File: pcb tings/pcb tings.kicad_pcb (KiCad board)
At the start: 2 copper layers, 24 parts, among them SW1 SW_Push, U1 ATmega32U4-A, Y1 16MHz

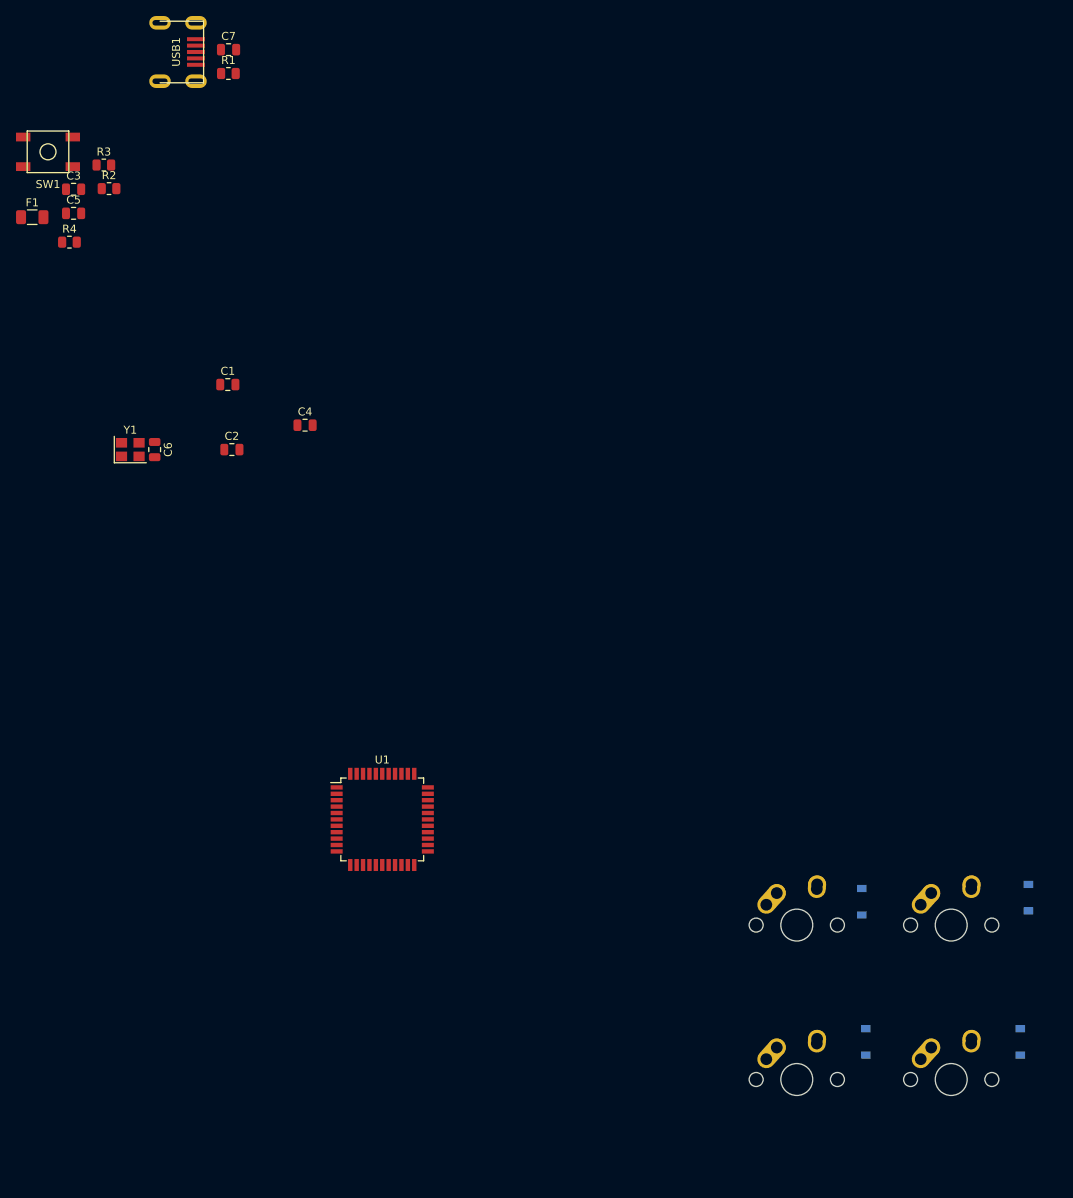
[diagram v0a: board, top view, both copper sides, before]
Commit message: completing the component placements.
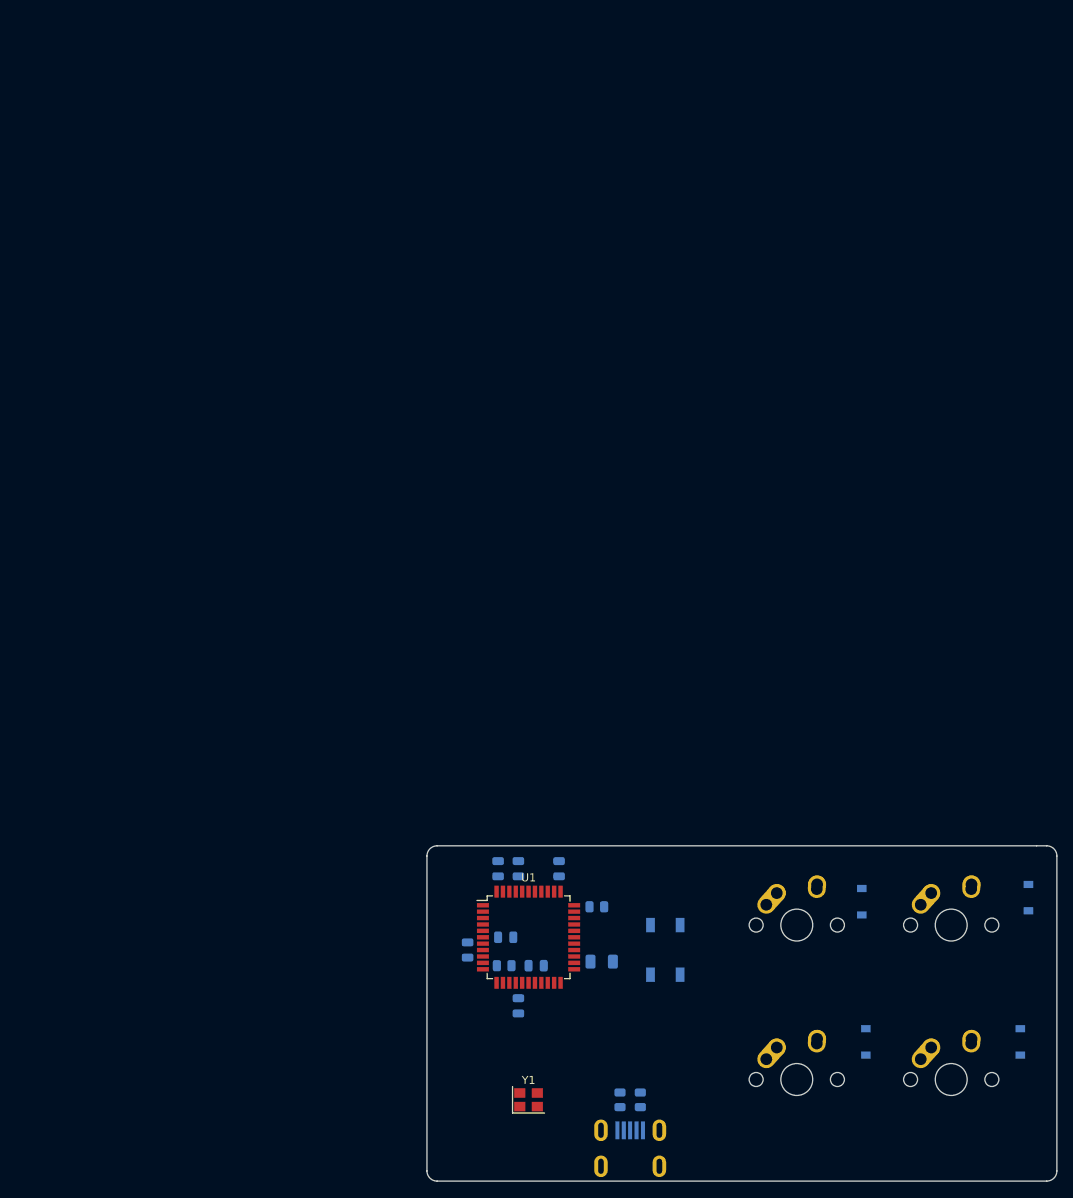
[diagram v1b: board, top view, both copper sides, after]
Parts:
- C1, C2, C3, C4, C5, C6, C7, F1, R1, R2, R3, R4, SW1, USB1: moved to B.Cu
- moved USB1 151.2 mm to (142.2, 112.5), turned to 90 degrees
- moved R1 137.3 mm to (141.0, 104.1), turned to -90 degrees
- moved R2 131.8 mm to (143.5, 104.1), turned to -90 degrees
- moved SW1 126.1 mm to (146.6, 85.4), turned to 90 degrees
- moved F1 117.2 mm to (138.7, 86.9), turned to 180 degrees
- moved C7 116.2 mm to (126.7, 83.8)
- moved C3 113.0 mm to (130.5, 87.4), turned to 180 degrees
- moved R3 111.9 mm to (126.5, 87.4), turned to 180 degrees
- moved R4 106.1 mm to (138.1, 80.0)
- moved C5 99.0 mm to (128.3, 75.2), turned to 90 degrees
- moved Y1 95.3 mm to (129.5, 104.1)
- moved C4 77.3 mm to (128.3, 92.4), turned to 90 degrees
- moved C6 73.8 mm to (121.9, 85.4), turned to 90 degrees
- moved C1 73.3 mm to (133.3, 75.2), turned to 90 degrees
- moved C2 62.1 mm to (125.7, 75.2), turned to 90 degrees
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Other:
- board outline added: 78.7 x 41.9 mm

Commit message: Merge branch 'master' of https://github.com/maksemakes/4k-noob into rin_branch
# Conflicts:
#	pcb tings/pcb tings.kicad_pcb
#	pcb tings/pcb tings.kicad_sch
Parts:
- moved D2 1.83 mm to (190.5, 77.8)
- moved D1 1.65 mm to (171.2, 77.7)
- moved D4 0.51 mm to (190.5, 96.9)
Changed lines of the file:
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@@
   )
   (footprint "Diode_SMD:D_SOD-123" (layer "B.Cu")
-    (at 192.024 78.866 90)
+    (at 190.5 77.85 90)
     (descr "SOD-123")
     (tags "SOD-123")
@@
   )
   (footprint "Diode_SMD:D_SOD-123" (layer "B.Cu")
-    (at 191.008 96.902 90)
+    (at 190.5 96.902 90)
     (descr "SOD-123")
     (tags "SOD-123")
@@
   )
   (footprint "Diode_SMD:D_SOD-123" (layer "B.Cu")
-    (at 171.196 79.374 90)
+    (at 171.196 77.724 90)
     (descr "SOD-123")
     (tags "SOD-123")
